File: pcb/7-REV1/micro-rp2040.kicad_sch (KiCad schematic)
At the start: 60 parts, among them J201 Conn_01x03, J202 TYPE-C-31-M-12, Q1 2N7002T, Q5 2N7002T, SW101 TS3425BA 098 2.5H 250gf, SW102 TS3315A 250gf 025, U1 RP2350B, U102 W25Q128JVSIQ, U105 MT29F1G01ABAFDWB, U16 SP3002-04JTG, U3 TLV74311PDBVR, U401 ME6211A33PG-N, U8 APS6404L-3SQR-ZR, Y101 ABM8-272-T3

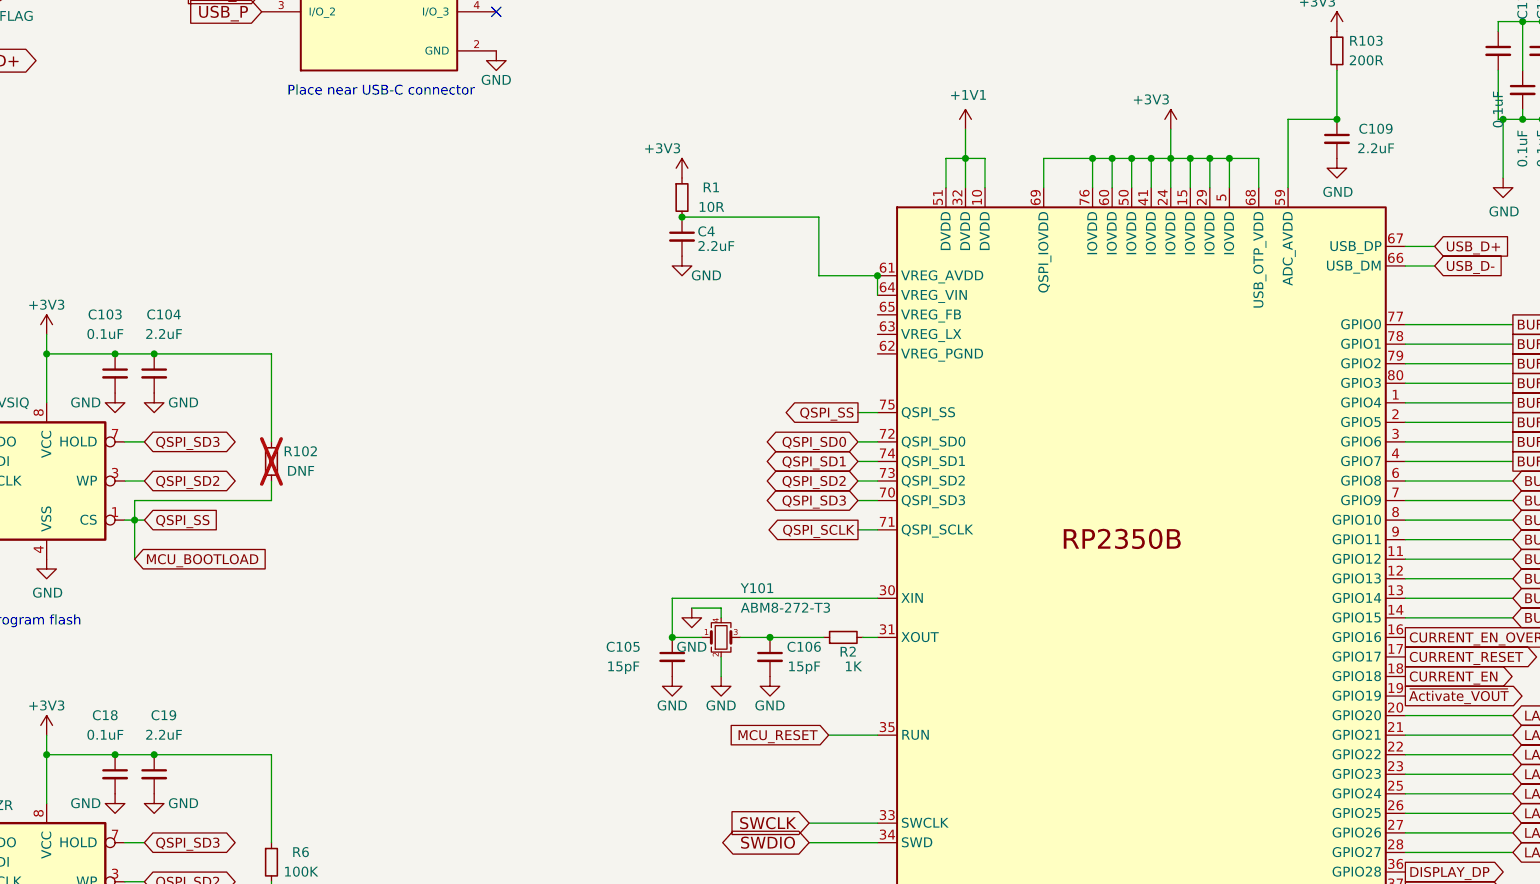
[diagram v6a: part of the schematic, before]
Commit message: TCA6416ARTWR IO expander, 2.2uF->4.7uF
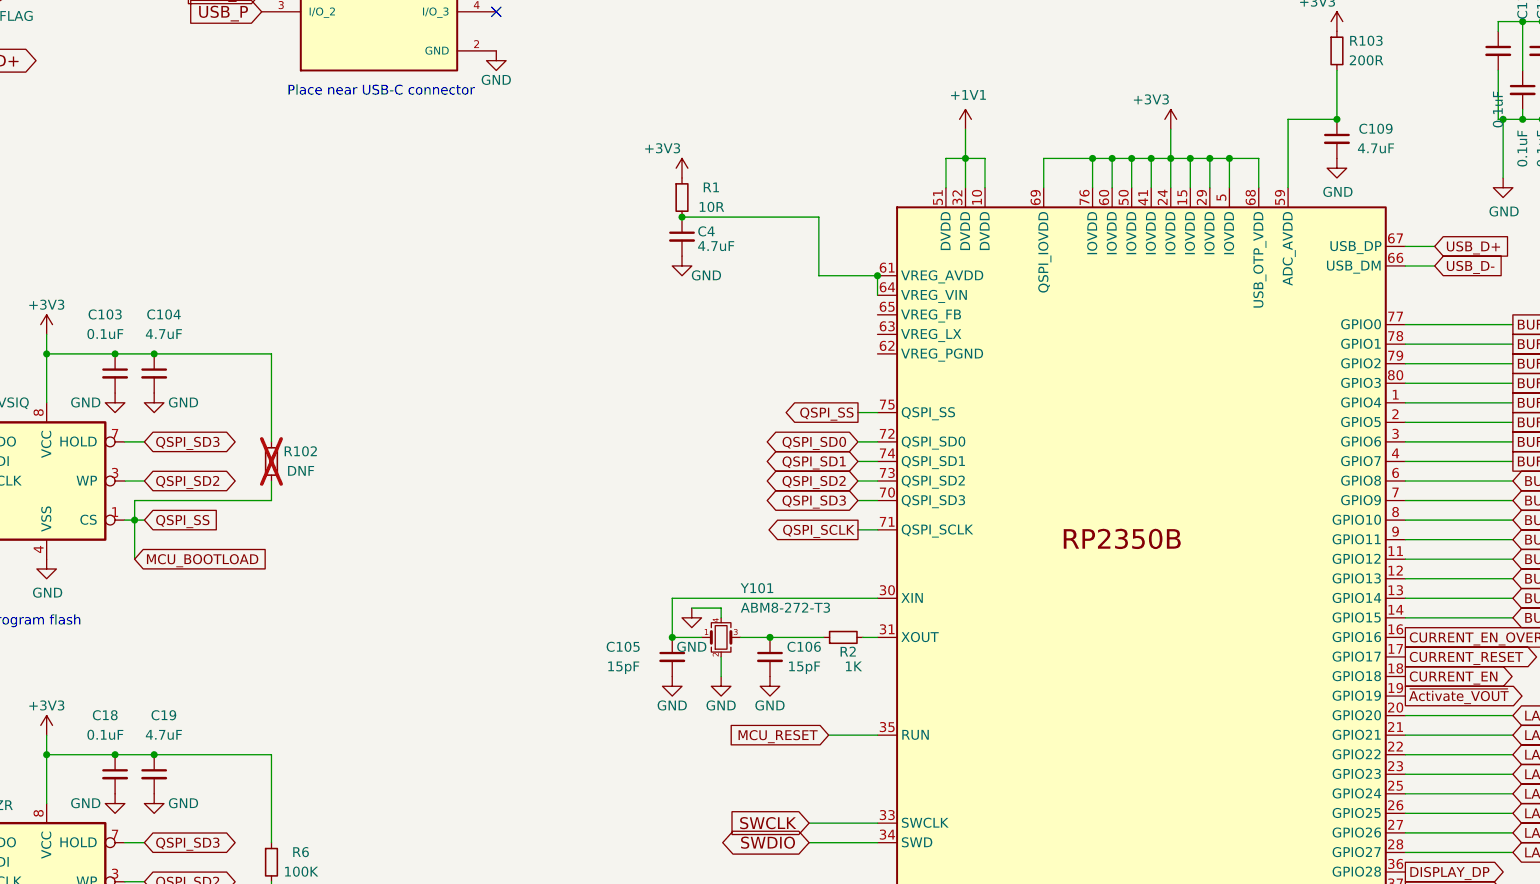
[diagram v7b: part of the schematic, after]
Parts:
- C104, C109, C19, C4: value 2.2uF -> 4.7uF
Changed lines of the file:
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@@
 			)
 		)
-		(property "Value" "2.2uF"
+		(property "Value" "4.7uF"
 			(at 135.89 82.55 0)
 			(effects
@@
 			)
 		)
-		(property "Value" "2.2uF"
+		(property "Value" "4.7uF"
 			(at 293.37 58.42 0)
 			(effects
@@
 			)
 		)
-		(property "Value" "2.2uF"
+		(property "Value" "4.7uF"
 			(at 135.89 134.62 0)
 			(effects
@@
 			)
 		)
-		(property "Value" "2.2uF"
+		(property "Value" "4.7uF"
 			(at 207.645 71.12 0)
 			(effects

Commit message: BP7REV1 2.2uF, 4.7uF-> 10uF/6.3V CL05A106MQ5NUN. 520K->470K on reset/bootloader switch.
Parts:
- C10, C104, C109, C11, C19, C201, C202, C24, C36, C4, C401, C402: value 4.7uF -> 10uF/6.3v
- R10: value 560k -> 470K
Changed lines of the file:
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@@
 			)
 		)
-		(property "Value" "4.7uF"
+		(property "Value" "10uF/6.3v"
 			(at 365.76 68.58 0)
 			(effects
@@
 			)
 		)
-		(property "Description" ""
+		(property "Description" "CL05A106MQ5NUN"
 			(at 368.3 67.31 0)
 			(effects
@@
 			)
 		)
-		(property "Value" "4.7uF"
+		(property "Value" "10uF/6.3v"
 			(at 396.0368 68.453 0)
 			(effects
@@
 			)
 		)
-		(property "Description" ""
+		(property "Description" "CL05A106MQ5NUN"
 			(at 393.7 67.31 0)
 			(effects
@@
 			)
 		)
-		(property "Value" "4.7uF"
+		(property "Value" "10uF/6.3v"
 			(at 121.92 22.86 90)
 			(effects
@@
 			)
 		)
-		(property "Description" ""
+		(property "Description" "CL05A106MQ5NUN"
 			(at 113.03 22.86 0)
 			(effects
@@
 			)
 		)
-		(property "Value" "4.7uF"
+		(property "Value" "10uF/6.3v"
 			(at 121.92 29.21 90)
 			(effects
@@
 			)
 		)
-		(property "Description" ""
+		(property "Description" "CL05A106MQ5NUN"
 			(at 113.03 26.67 0)
 			(effects
@@
 			)
 		)
-		(property "Value" "4.7uF"
+		(property "Value" "10uF/6.3v"
 			(at 135.89 82.55 0)
 			(effects
@@
 			)
 		)
-		(property "Description" ""
+		(property "Description" "CL05A106MQ5NUN"
 			(at 134.62 87.63 0)
 			(effects
@@
 			)
 		)
-		(property "Value" "4.7uF"
+		(property "Value" "10uF/6.3v"
 			(at 293.37 58.42 0)
 			(effects
@@
 			)
 		)
-		(property "Description" ""
+		(property "Description" "CL05A106MQ5NUN"
 			(at 288.29 57.15 0)
 			(effects
@@
 			)
 		)
-		(property "Value" "4.7uF"
+		(property "Value" "10uF/6.3v"
 			(at 135.89 134.62 0)
 			(effects
@@
 			)
 		)
-		(property "Description" ""
+		(property "Description" "CL05A106MQ5NUN"
 			(at 134.62 139.7 0)
 			(effects
@@
 			)
 		)
-		(property "Value" "4.7uF"
+		(property "Value" "10uF/6.3v"
 			(at 365.76 41.91 0)
 			(effects
@@
 			)
 		)
-		(property "Description" ""
+		(property "Description" "CL05A106MQ5NUN"
 			(at 368.3 40.64 0)
 			(effects
@@
 			)
 		)
-		(property "Value" "4.7uF"
+		(property "Value" "10uF/6.3v"
 			(at 46.99 143.256 0)
 			(effects
@@
 			)
 		)
-		(property "Value" "560k"
+		(property "Value" "470K"
 			(at 39.37 140.97 0)
 			(effects
@@
 			)
 		)
-		(property "Value" "4.7uF"
+		(property "Value" "10uF/6.3v"
 			(at 207.645 71.12 0)
 			(effects
@@
 			)
 		)
-		(property "Description" ""
+		(property "Description" "CL05A106MQ5NUN"
 			(at 203.2 69.85 0)
 			(effects
@@
 			)
 		)
-		(property "Value" "4.7uF"
+		(property "Value" "10uF/6.3v"
 			(at 188.468 33.02 90)
 			(effects
@@
 			)
 		)
-		(property "Description" ""
+		(property "Description" "CL05A106MQ5NUN"
 			(at 184.15 33.02 0)
 			(effects
@@
 			)
 		)
-		(property "Value" "4.7uF"
+		(property "Value" "10uF/6.3v"
 			(at 396.0368 41.783 0)
 			(effects
@@
 			)
 		)
-		(property "Description" ""
+		(property "Description" "CL05A106MQ5NUN"
 			(at 393.7 40.64 0)
 			(effects
